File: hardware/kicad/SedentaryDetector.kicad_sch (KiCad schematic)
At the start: 1 part, among them J1 Conn_02x09

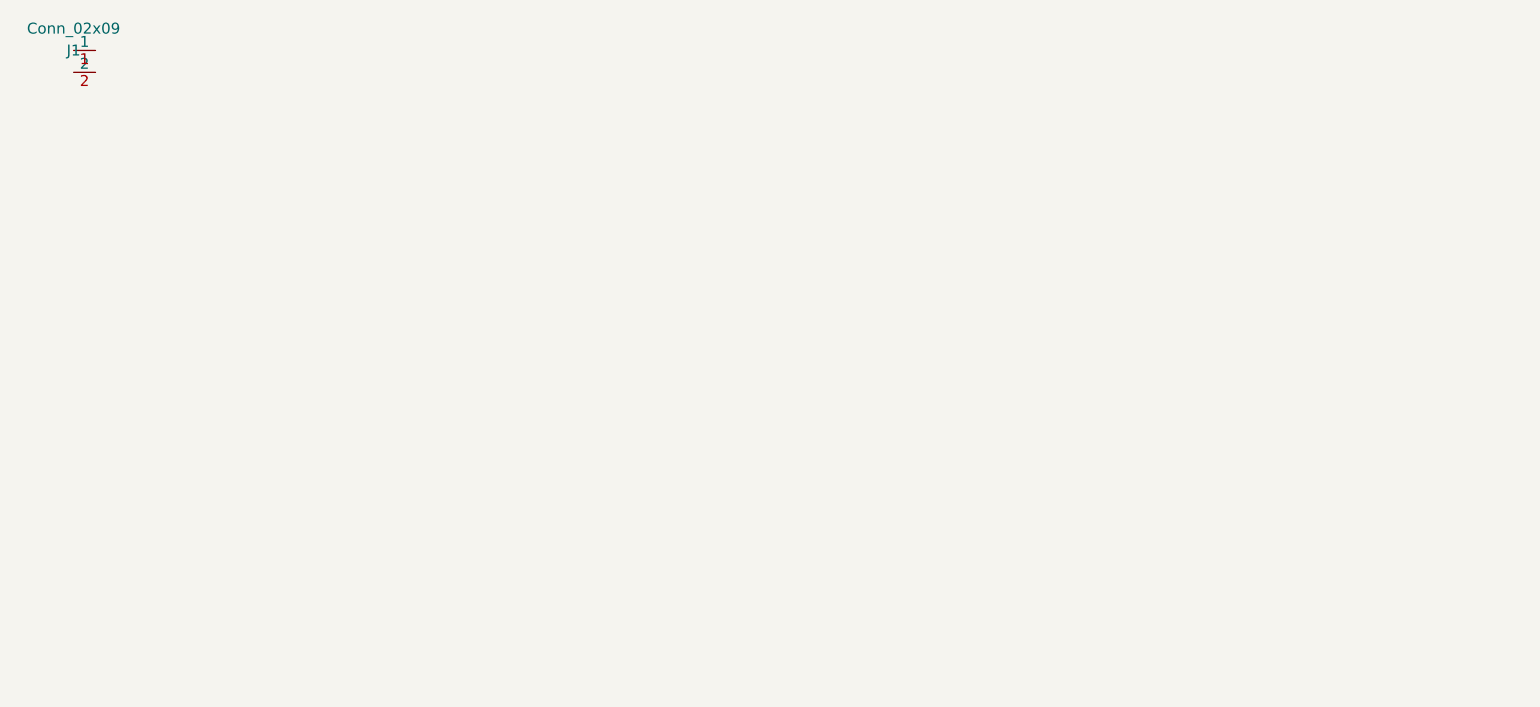
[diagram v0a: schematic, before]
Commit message: fix(schematic): generate valid KiCad 10 schematic
Replace broken gen_sch.py output with proper KiCad 10 format:
- J1: 2x15 ESP32-WROOM-32 connector (30 pins, inline symbol)
- J2: 1x8 MPU6050-GY521 connector (8 pins, inline symbol)
- Uses tab indentation (KiCad 10 requirement)
- Pin UUIDs generated properly
- Exports to PDF successfully
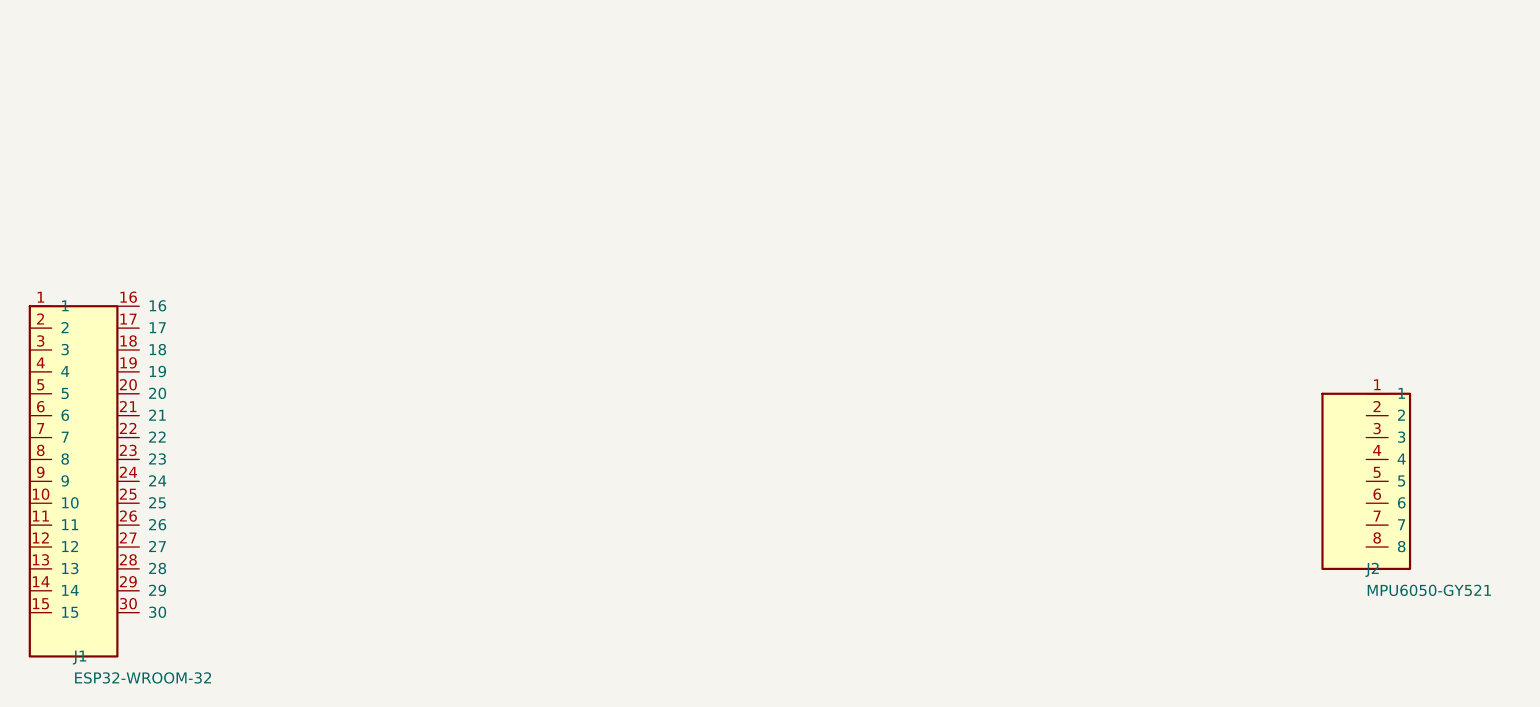
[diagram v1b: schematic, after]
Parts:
- removed J1: Conn_02x09, symbol Test:J1
- added J1: ESP32-WROOM-32, Connector_PinSocket_2.54mm:PinSocket_2x15_P2.54mm_Vertical, symbol Conn_02x15
- added J2: MPU6050-GY521, Connector_PinSocket_2.54mm:PinSocket_1x08_P2.54mm_Vertical, symbol Conn_01x08
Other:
- company: (none) -> Personal Project
- title: Test -> Sedentary Detector - Carrier Board
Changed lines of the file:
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@@
 (kicad_sch (version 20250114) (generator "eeschema")
-	(paper "A4")
+	(paper "A3")
 	(title_block
-		(title "Test")
+		(title "Sedentary Detector - Carrier Board")
 		(date "2026-06-20")
+		(rev "0.1")
+		(company "Personal Project")
 	)
-	(symbol (lib_id "Test:J1") (at 50 50 0) (unit 1) (in_bom yes) (on_board yes)
-		(property "Reference" "J1" (at 50 50 0) (effects (font (size 1.27 1.27))))
-		(property "Value" "Conn_02x09" (at 50 47.46 0) (effects (font (size 1.27 1.27))))
-		(property "Footprint" "" (at 50 50 0) (effects (font (size 1.27 1.27)) hide))
-		(property "Datasheet" "" (at 50 50 0) (effects (font (size 1.27 1.27)) hide))
+	(symbol (lib_id "Conn_02x15") (at 50 100 0) (unit 1) (in_bom yes) (on_board yes)
+		(property "Reference" "J1" (at 50 120.32 0)
+			(effects (font (size 1.27 1.27)) (justify left))
+		)
+		(property "Value" "ESP32-WROOM-32" (at 50 122.86 0)
+			(effects (font (size 1.27 1.27)) (justify left))
+		)
+		(property "Footprint" "Connector_PinSocket_2.54mm:PinSocket_2x15_P2.54mm_Vertical" (at 50 80 0)
+			(effects (font (size 1.27 1.27)) (hide yes))
+		)
+		(property "Datasheet" "~" (at 50 80 0)
+			(effects (font (size 1.27 1.27)) (hide yes))
+		)
 		(pin "1")
 		(pin "2")
+		(pin "3")
+		(pin "4")
+		(pin "5")
+		(pin "6")
+		(pin "7")
+		(pin "8")
+		(pin "9")
+		(pin "10")
+		(pin "11")
+		(pin "12")
+		(pin "13")
+		(pin "14")
+		(pin "15")
+		(pin "16")
+		(pin "17")
+		(pin "18")
+		(pin "19")
+		(pin "20")
+		(pin "21")
+		(pin "22")
+		(pin "23")
+		(pin "24")
+		(pin "25")
+		(pin "26")
+		(pin "27")
+		(pin "28")
+		(pin "29")
+		(pin "30")
+	)
+	(symbol (lib_id "Conn_01x08") (at 200 100 0) (unit 1) (in_bom yes) (on_board yes)
+		(property "Reference" "J2" (at 200 110.16 0)
+			(effects (font (size 1.27 1.27)) (justify left))
+		)
+		(property "Value" "MPU6050-GY521" (at 200 112.7 0)
+			(effects (font (size 1.27 1.27)) (justify left))
+		)
+		(property "Footprint" "Connector_PinSocket_2.54mm:PinSocket_1x08_P2.54mm_Vertical" (at 200 90 0)
+			(effects (font (size 1.27 1.27)) (hide yes))
+		)
+		(property "Datasheet" "~" (at 200 90 0)
+			(effects (font (size 1.27 1.27)) (hide yes))
+		)
+		(pin "1")
+		(pin "2")
+		(pin "3")
+		(pin "4")
+		(pin "5")
+		(pin "6")
+		(pin "7")
+		(pin "8")
+	)
+	(sheet_instances
+		(path "/" (page "1"))
 	)
 )
